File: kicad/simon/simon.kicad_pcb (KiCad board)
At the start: 2 copper layers, 99.8 x 99.8 mm, 20 parts, among them J1 GPIO, J2 Power, U1 74LS06

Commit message: Production version of Simon board.
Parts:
- moved U1 45.1 mm to (156.5, 83.6)
- moved S2 20.6 mm to (212.8, 114.3)
- moved R5 20.4 mm to (201.7, 75.4)
- moved S1 20.4 mm to (212.8, 72.6)
- moved R1 20.4 mm to (214.6, 78.2)
- moved R7 20.3 mm to (201.7, 117.1)
- moved R2 20.1 mm to (204.5, 104.1)
- moved S3 20.0 mm to (147.3, 114.3)
- moved R9 19.9 mm to (151.9, 106.9)
- moved R3 19.5 mm to (138.9, 104.1)
- moved R4 19.4 mm to (149.1, 78.2)
- moved S4 19.4 mm to (147.3, 72.6)
- moved R11 19.4 mm to (151.9, 65.3)
- moved J2 17.6 mm to (177.5, 62.7), turned to 90 degrees
- moved R6 15.2 mm to (191.0, 83.6)
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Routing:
- net VCC: track 269.0 -> 185.2 mm
- net GND: track 251.0 -> 178.6 mm
- net Net-(S3-K): track 77.9 -> 19.6 mm
- net Net-(S4-K): track 83.0 -> 36.8 mm
- net LT3: track 38.7 -> 74.3 mm
- net LT2: track 45.4 -> 73.3 mm
- net LT0: track 48.2 -> 68.8 mm
- net SW1: track 65.4 -> 48.4 mm
- net LT1: track 49.4 -> 64.9 mm
- net Net-(S1-K): track 52.1 -> 67.3 mm
- net SW3: track 93.0 -> 78.5 mm
- net SW0: track 44.7 -> 36.3 mm
- net SW2: track 104.0 -> 97.9 mm, vias 0 -> 1
- net Net-(S2-K): track 72.2 -> 71.6 mm
- net Net-(S3-A): track 7.59 -> 7.08 mm
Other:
- board size 99.8 x 99.8 mm -> 91.4 x 62 mm
- board text added: "+5"
- board text added: "GND"

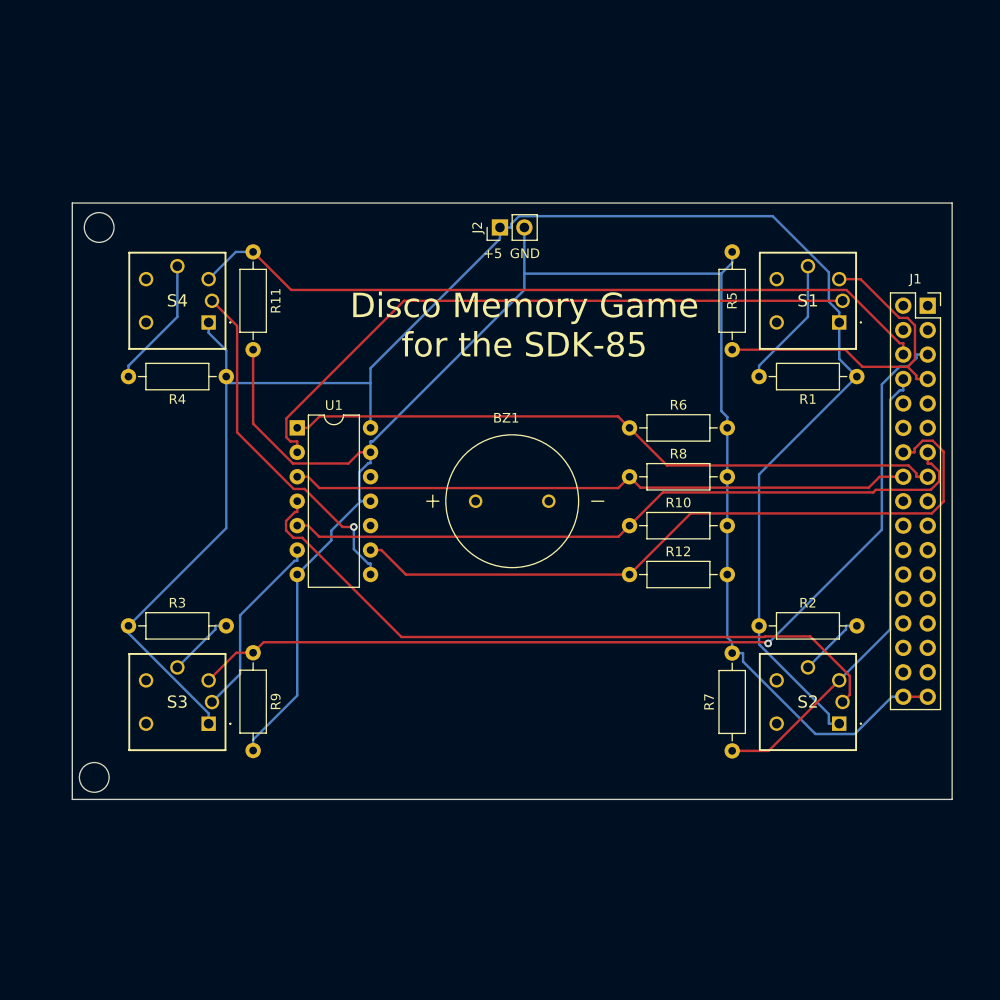
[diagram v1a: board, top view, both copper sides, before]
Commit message: Fixed trace routing to speaker.  This is the real production version.
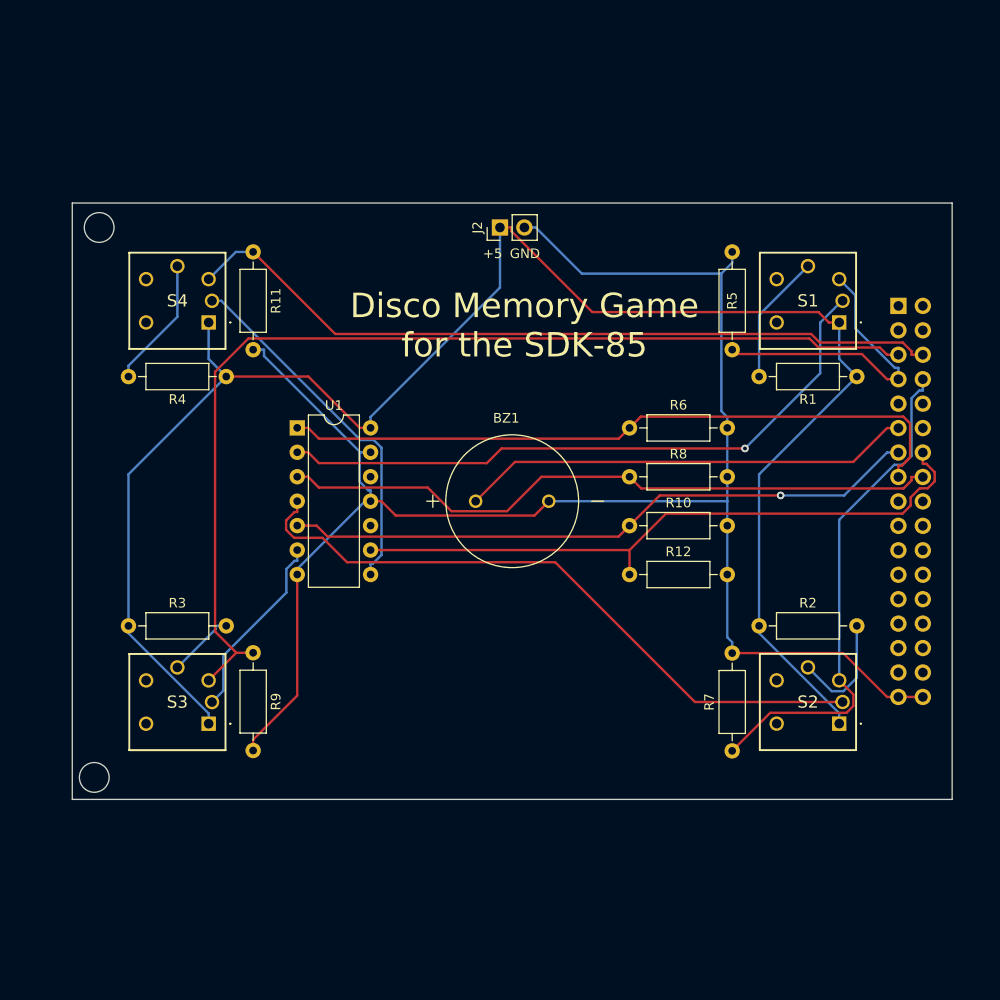
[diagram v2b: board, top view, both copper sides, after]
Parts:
- BZ1: footprint buzzer:XDCR_AT-1438-TWT-R -> parts:XDCR_AT-1438-TWT-R
- J1: moved to B.Cu
- S1, S2, S3, S4: footprint omron:B3W9002Y1Y -> parts:B3W9002Y1Y
- moved J1 3.05 mm to (218.9, 70.9), turned to 180 degrees
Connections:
- J1 pad 11: Net-(BZ1--) -> /SPKR
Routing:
- net /SPKR: track 0.00 -> 47.1 mm
- net SW2: track 97.9 -> 109.1 mm, vias 1 -> 0
- net LT2: track 73.3 -> 66.6 mm, vias 0 -> 1
- net LT3: track 74.3 -> 68.3 mm
- net Net-(S2-A): track 7.07 -> 12.1 mm
- net SW1: track 48.4 -> 53.4 mm
- net SW0: track 36.3 -> 31.7 mm
- net LT1: track 64.9 -> 69.2 mm
- net LT0: track 68.8 -> 71.7 mm
- net Net-(S2-K): track 71.6 -> 68.9 mm
- net VCC: track 185.2 -> 183.4 mm
- net SW3: track 78.5 -> 80.0 mm
- net Net-(S4-K): track 36.8 -> 37.7 mm, vias 1 -> 0
- net GND: track 178.6 -> 179.3 mm
- net Net-(S1-K): track 67.3 -> 67.2 mm, vias 0 -> 1

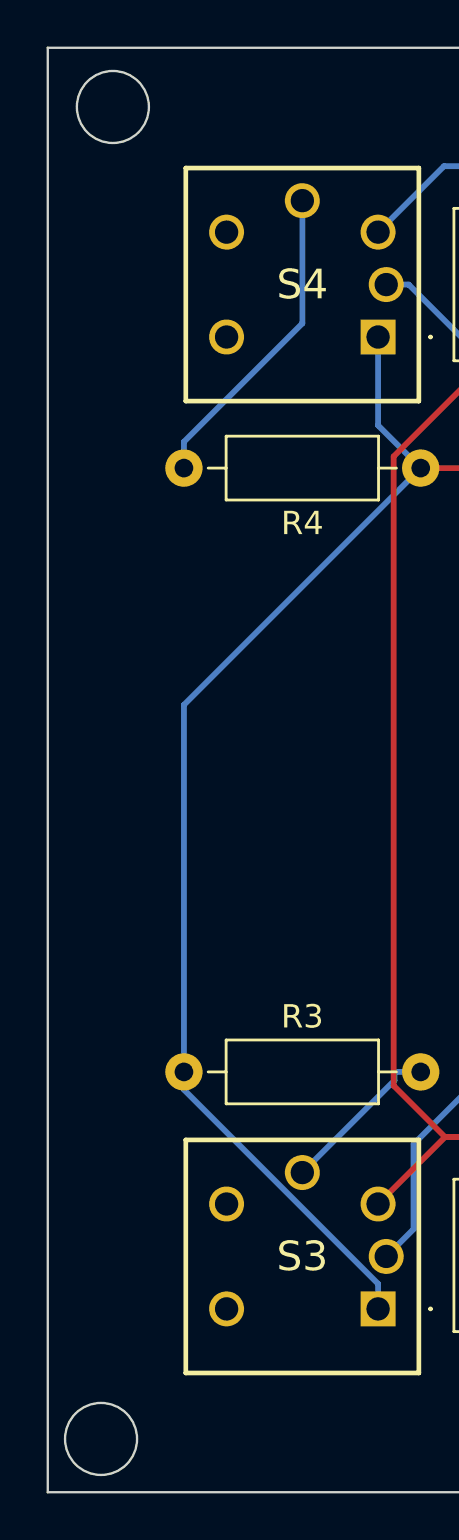
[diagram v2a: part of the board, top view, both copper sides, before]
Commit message: Updated board with larger holes, BOM, and part numbers. This corresponds to the community shared version (v1.0.1)
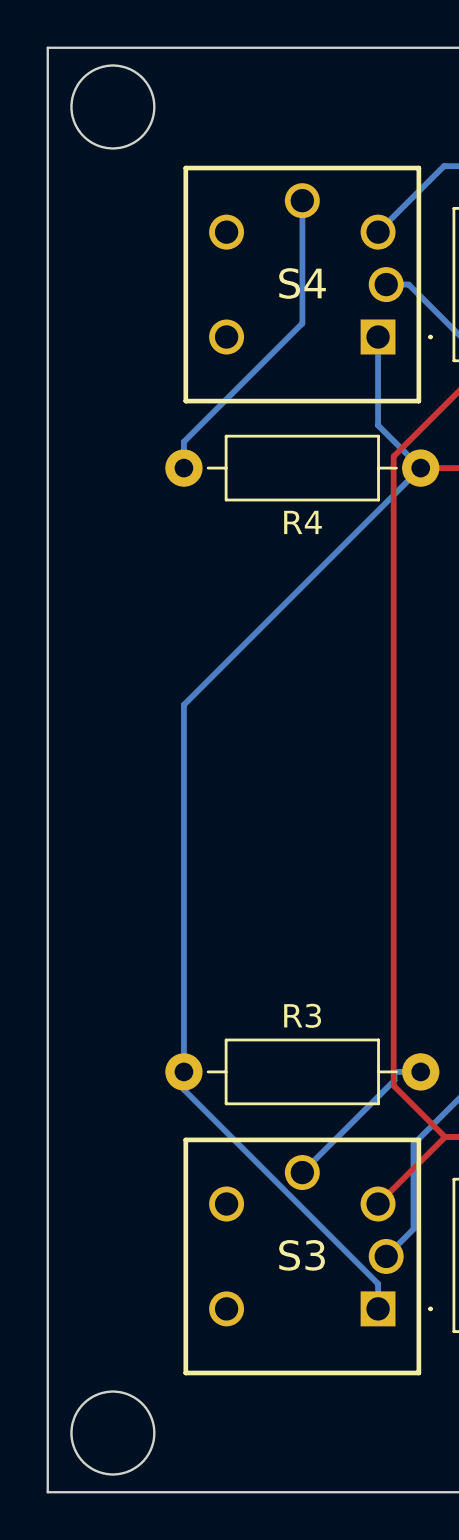
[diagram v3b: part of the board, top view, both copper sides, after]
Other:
- outline, holes or cut-outs redrawn
- board text added: "https://github.com/jimshortz/sdk-85 v1.0.1 - Oct 2023"
- board text removed: "https://github.com/jimshortz/sdk-85 v1.0 - Oct 2023"
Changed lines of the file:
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@@
   )
   (paper "USLetter")
+  (title_block
+    (title "Disco Memory Game for SDK-85")
+    (date "2023-10-22")
+    (company "Jim Shortz")
+  )
   (layers
     (0 "F.Cu" signal)
@@
     )
   )
-  (gr_circle (center 135.89 62.738) (end 137.414 62.992)
+  (gr_circle (center 135.89 62.738) (end 137.668 62.738)
     (stroke (width 0.1) (type default)) (fill none) (layer "Edge.Cuts"))
   (gr_rect (start 133.096 60.198) (end 224.536 122.174)
     (stroke (width 0.1) (type default)) (fill none) (layer "Edge.Cuts"))
-  (gr_circle (center 135.382 119.888) (end 136.906 120.142)
+  (gr_circle (center 135.89 119.634) (end 137.668 119.634)
     (stroke (width 0.1) (type default)) (fill none) (layer "Edge.Cuts"))
   (gr_text "GND" (at 178.562 66.04) (layer "F.SilkS")
@@
     (effects (font (size 1 1) (thickness 0.15)) (justify left bottom))
   )
-  (gr_text "https://github.com/jimshortz/sdk-85\nv1.0 - Oct 2023" (at 178.308 118.872) (layer "Edge.Cuts")
+  (gr_text "https://github.com/jimshortz/sdk-85\nv1.0.1 - Oct 2023" (at 178.308 118.872) (layer "Edge.Cuts")
     (effects (font (size 1.27 1.27) (thickness 0.1905)) (justify bottom))
   )
